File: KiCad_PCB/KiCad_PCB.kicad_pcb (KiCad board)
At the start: 4 copper layers, 50 x 50 mm, 33 parts, among them J1 Conn_01x04, J2 USB-C31-S-RA-CS2-SMT-BK-T/R, U1 LT3021ES8, U2 NRF52832-QFAA-R, Y1 ECS-320-8-33B-7KM-TR, Y2 ECS-.327-12.5-12R-TR

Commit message: Updated KiCad project
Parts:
- moved L2 3.09 mm to (138.2, 85.6)
- moved C10 2.39 mm to (134.4, 84.8), turned to -90 degrees
- moved C9 1.87 mm to (134.9, 80.9)
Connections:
- E1 pad 1: Net-(C10-Pad1) -> Net-(E1-Pad1)
- L2 pad 2: Net-(C10-Pad1) -> Net-(E1-Pad1)
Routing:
- net Net-(E1-Pad1): track 0.00 -> 18.4 mm
- net Net-(C10-Pad1): track 26.7 -> 9.45 mm
- net GND: track 0.00 -> 12.5 mm
- net +5V: track 13.6 -> 25.9 mm, vias 0 -> 5
- net +1V8: track 36.0 -> 46.4 mm, vias 0 -> 4
- net Net-(C9-Pad2): track 3.13 -> 4.99 mm
- net (no net): vias 8 -> 0

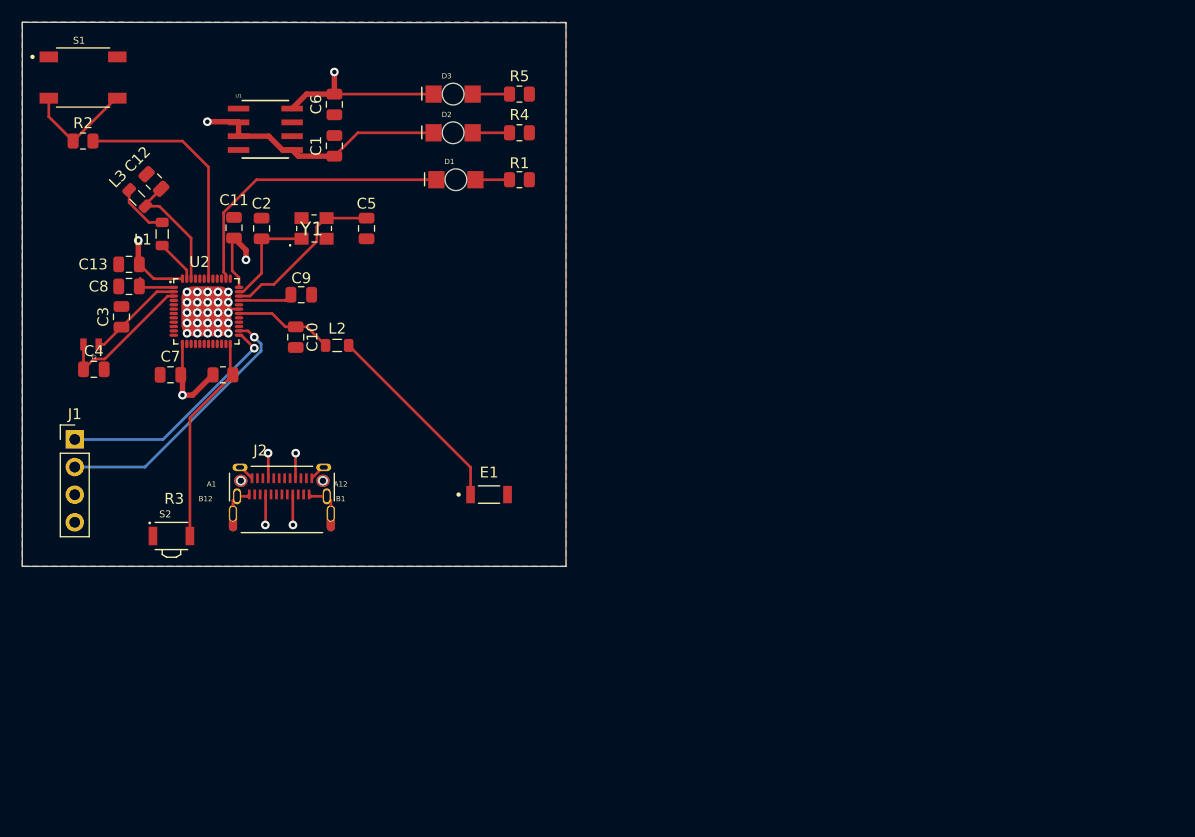
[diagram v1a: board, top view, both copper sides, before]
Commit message: Updated footprints and added battery holder on KiCad project
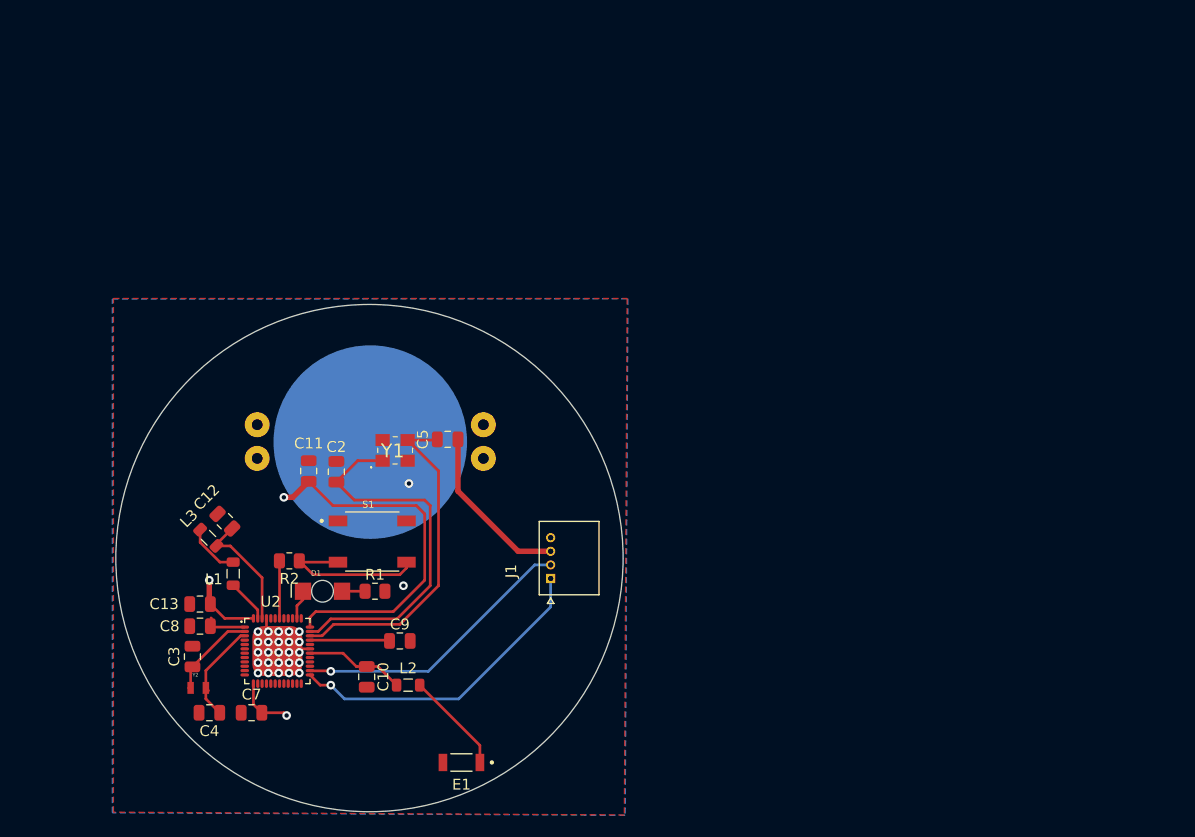
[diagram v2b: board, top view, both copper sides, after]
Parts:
- removed C1, C6: 3.3u, Capacitor_SMD:C_0805_2012Metric
- removed D2, D3: 597-3111-407F, componentes:LEDC3216X110N
- removed J2: USB-C31-S-RA-CS2-SMT-BK-T/R, componentes:ADAM_USB-C31-S-RA-CS2-SMT-BK-T_R
- removed R3: 1k, Resistor_SMD:R_0805_2012Metric
- removed R4, R5: 200, Resistor_SMD:R_0805_2012Metric
- removed S2: B3U-3000P, componentes:SW_B3U-3000P
- removed U1: LT3021ES8, componentes:SO-8_S
- added BT1: BAT-HLD-001-THM-TR, componentes:BAT_BAT-HLD-001-THM-TR, B.Cu at (141.2, 94.5)
- J1: value Conn_01x04 -> 530480450; footprint Connector_PinHeader_2.54mm:PinHeader_1x04_P2.54mm_Vertical -> componentes:MOLEX_530480450
- moved S1 50.3 mm to (141.4, 103.6)
- moved J1 45.6 mm to (157.8, 107.0), turned to 90 degrees
- moved R2 43.0 mm to (133.8, 105.4), turned to 180 degrees
- moved R1 40.1 mm to (141.7, 108.2)
- moved D1 39.8 mm to (136.8, 108.2)
- moved C4 33.3 mm to (126.4, 119.4), turned to 180 degrees
- moved C9 33.1 mm to (143.9, 112.8)
- moved Y2 33.1 mm to (125.4, 117.1), turned to 0 degrees
- moved C7 32.0 mm to (130.3, 119.4)
- moved C12 31.9 mm to (127.9, 101.8)
- moved C13 31.9 mm to (125.6, 109.4)
- moved C8 31.9 mm to (125.6, 111.4)
- moved L1 31.9 mm to (128.6, 106.6)
- moved L2 31.9 mm to (144.7, 116.8)
- moved L3 31.9 mm to (126.3, 103.3)
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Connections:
- J1 pad 3: +1V8 -> GND
- J1 pad 4: GND -> +1V8
- U2 pad 24: Net-(R3-Pad1) -> unconnected-(U2-Pad24)
- U2 pad 45: unconnected-(U2-Pad45) -> GND
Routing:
- net +5V: track 25.9 -> 0.00 mm, vias 5 -> 0
- net ECS-320_XCS2: track 9.63 -> 34.8 mm
- net Net-(D1-PadA): track 27.0 -> 2.73 mm
- net Net-(R3-Pad1): track 20.0 -> 0.00 mm
- net Net-(R2-Pad2): track 21.9 -> 5.29 mm
- net Net-(C5-Pad2): track 15.5 -> 31.1 mm
- net Net-(E1-Pad1): track 18.4 -> 9.41 mm
- net PROG_SWCLK: track 21.9 -> 29.4 mm
- net GND: track 12.5 -> 20.0 mm, vias 25 -> 27
- net Net-(R2-Pad1): track 10.6 -> 14.8 mm
- net Net-(C4-Pad1): track 13.4 -> 9.66 mm
- net Net-(D3-PadC): track 3.39 -> 0.00 mm
- net Net-(D2-PadC): track 3.39 -> 0.00 mm
- net Net-(C9-Pad2): track 4.99 -> 7.35 mm
- net PROG_SWDIO: track 24.7 -> 26.2 mm
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- removed copper zone on In2.Cu, net +5V
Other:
- board size 50 x 50 mm -> 46.7 x 46.7 mm

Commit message: Tutorías 10/3
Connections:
- J1 pad 1: PROG_SWCLK -> GND
- J1 pad 3: GND -> PROG_SWCLK
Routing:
- net GND: track 20.0 -> 4.38 mm, vias 27 -> 47
- net +1V8: track 46.1 -> 53.4 mm
- net PROG_SWCLK: track 29.4 -> 26.8 mm
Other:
- board size 46.7 x 46.7 mm -> 97.2 x 46.7 mm

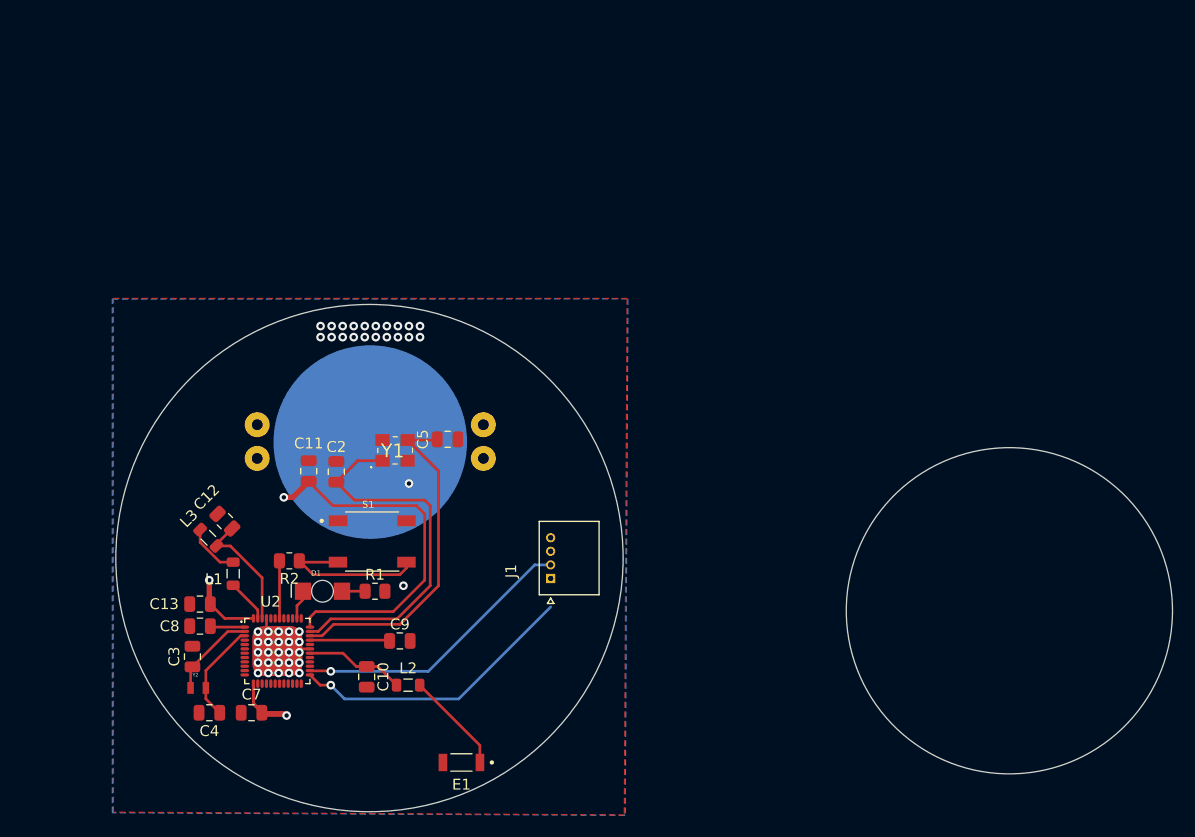
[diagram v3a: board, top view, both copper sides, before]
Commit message: PCB size reduced
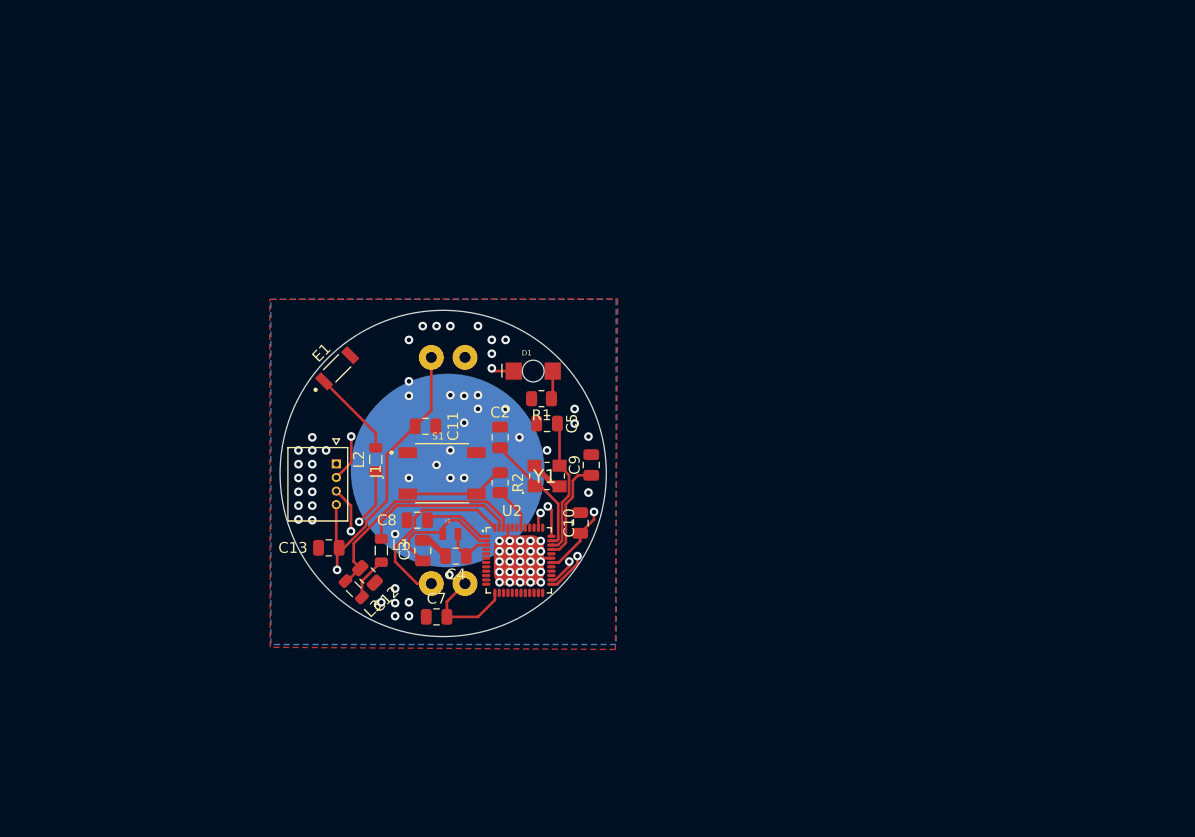
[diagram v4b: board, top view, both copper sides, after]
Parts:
- moved E1 38.0 mm to (138.2, 87.7), turned to 45 degrees
- moved D1 28.0 mm to (156.2, 88.0)
- moved Y2 27.2 mm to (148.6, 102.9)
- moved C4 26.9 mm to (149.1, 105.0)
- moved C10 24.2 mm to (160.5, 101.9), turned to 90 degrees
- moved C9 23.9 mm to (161.5, 96.6), turned to -90 degrees
- moved U2 23.7 mm to (154.9, 105.4)
- moved R1 23.4 mm to (157.0, 90.5), turned to 0 degrees
- moved C3 23.3 mm to (146.1, 104.5)
- moved J1 22.4 mm to (138.1, 96.5), turned to -90 degrees
- moved C8 22.2 mm to (145.5, 101.7)
- moved L2 21.0 mm to (141.7, 96.1), turned to 90 degrees
- moved R2 20.7 mm to (153.2, 98.2), turned to -90 degrees
- moved C7 19.2 mm to (147.3, 110.6)
- moved C2 15.4 mm to (153.2, 94.1)
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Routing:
- net Net-(C10-Pad1): track 9.45 -> 33.9 mm, vias 0 -> 2
- net ECS-320_XCS2: track 34.8 -> 11.7 mm
- net Net-(C5-Pad2): track 31.1 -> 12.6 mm
- net Net-(D1-PadA): track 2.73 -> 18.7 mm, vias 0 -> 2
- net PROG_SWDIO: track 26.2 -> 40.5 mm, vias 1 -> 2
- net Net-(L1-Pad1): track 3.99 -> 14.3 mm
- net Net-(C12-Pad1): track 11.3 -> 21.2 mm
- net GND: track 4.38 -> 10.2 mm, vias 47 -> 74
- net Net-(R2-Pad1): track 14.8 -> 9.29 mm
- net Net-(C4-Pad1): track 9.31 -> 4.60 mm
- net +1V8: track 53.4 -> 57.1 mm, vias 3 -> 2
- net PROG_SWCLK: track 26.8 -> 30.3 mm, vias 1 -> 2
- net Net-(C3-Pad1): track 8.16 -> 11.6 mm
- net Net-(C8-Pad2): track 3.20 -> 6.43 mm
- net Net-(C9-Pad2): track 7.35 -> 9.46 mm
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- added copper zone on In2.Cu, net GND
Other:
- board size 97.2 x 46.7 mm -> 30 x 30 mm

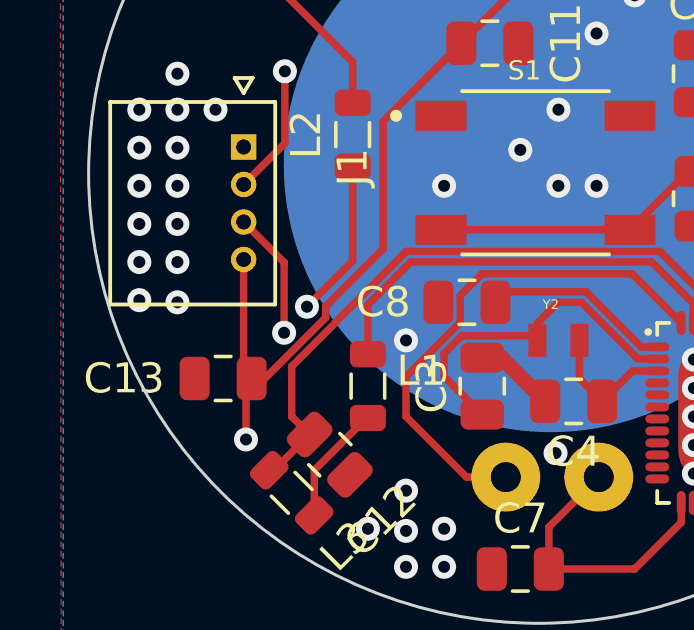
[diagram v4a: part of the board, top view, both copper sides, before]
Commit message: PCB size reduced
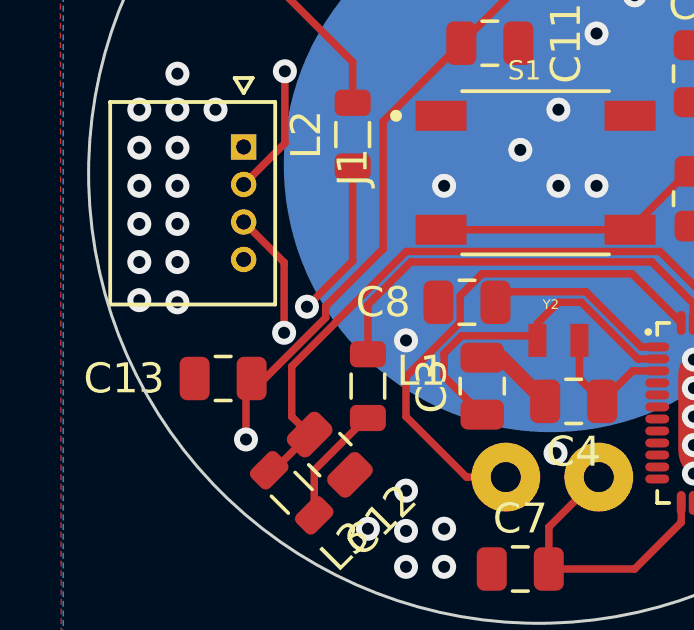
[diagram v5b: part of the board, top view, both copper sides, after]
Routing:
- net +1V8: track 57.1 -> 53.4 mm
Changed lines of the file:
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@@
   (segment (start 148.27 109.165788) (end 148.27 110.561788) (width 0.25) (layer "F.Cu") (net 1))
   (segment (start 145.354 93.035788) (end 142.748 95.641788) (width 0.25) (layer "F.Cu") (net 1))
-  (segment (start 138.098 100.244788) (end 138.098 103.945788) (width 0.25) (layer "F.Cu") (net 1))
   (segment (start 138.098 103.945788) (end 138.364 104.211788) (width 0.25) (layer "F.Cu") (net 1))
   (segment (start 138.805193 104.211788) (end 138.364 104.211788) (width 0.25) (layer "F.Cu") (net 1))

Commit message: Tutoría Modificacion PCB
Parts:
- C10, C11, C12, C2, C3, C4, C5, C7, C8: footprint Capacitor_SMD:C_0805_2012Metric -> Capacitor_SMD:C_0603_1608Metric
- C13, C9: footprint Capacitor_SMD:C_0805_2012Metric -> Capacitor_SMD:C_0603_1608Metric; moved to B.Cu
- R1, R2: footprint Resistor_SMD:R_0805_2012Metric -> Resistor_SMD:R_0603_1608Metric
- moved C13 21.2 mm to (158.2, 100.2), turned to -90 degrees
- moved L2 19.3 mm to (161.0, 96.5)
- moved R1 19.0 mm to (138.3, 94.1), turned to 180 degrees
- moved E1 19.0 mm to (157.1, 89.4), turned to 90 degrees
- moved D1 18.2 mm to (138.4, 91.8), turned to 180 degrees
- moved C12 15.1 mm to (153.4, 98.2), turned to 90 degrees
- moved L3 14.6 mm to (152.5, 101.0), turned to 0 degrees
- moved C11 10.2 mm to (147.7, 103.1), turned to 0 degrees
- moved L1 6.75 mm to (148.1, 101.1), turned to 0 degrees
- moved C7 5.67 mm to (153.0, 110.2), turned to 180 degrees
- moved R2 4.43 mm to (151.8, 94.0), turned to 0 degrees
- moved C9 4.18 mm to (159.4, 100.2)
- moved C5 4.05 mm to (158.0, 96.8)
- moved C8 3.91 mm to (145.4, 105.6), turned to 90 degrees
- moved C2 3.26 mm to (155.8, 96.0)
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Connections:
- J1 pad 2: PROG_SWDIO -> PROG_SWCLK
- J1 pad 3: PROG_SWCLK -> PROG_SWDIO
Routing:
- net +1V8: track 53.4 -> 19.6 mm, vias 2 -> 3
- net Net-(C10-Pad1): track 33.9 -> 10.9 mm, vias 2 -> 0
- net Net-(C12-Pad1): track 21.2 -> 3.93 mm
- net PROG_SWDIO: track 40.5 -> 27.0 mm, vias 2 -> 1
- net Net-(C3-Pad1): track 11.6 -> 4.94 mm
- net Net-(D1-PadA): track 18.7 -> 24.4 mm, vias 2 -> 0
- net Net-(R2-Pad2): track 4.02 -> 9.41 mm
- net Net-(C9-Pad2): track 9.46 -> 5.43 mm, vias 0 -> 1
- net Net-(C5-Pad2): track 12.6 -> 9.64 mm
- net GND: track 10.2 -> 7.75 mm, vias 74 -> 25
- net Net-(L1-Pad1): track 14.3 -> 12.0 mm
- net ECS-320_XCS2: track 11.7 -> 9.59 mm
- net Net-(E1-Pad1): track 8.09 -> 6.09 mm
- net Net-(L1-Pad2): track 4.01 -> 2.12 mm
- net Net-(R2-Pad1): track 9.29 -> 7.76 mm
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- removed copper zone on In1.Cu, net +1V8
- removed copper zone on B.Cu, net GND
- removed copper zone on F.Cu, net GND
- removed copper zone on In2.Cu, net GND
